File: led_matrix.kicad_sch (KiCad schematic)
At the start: 128 parts

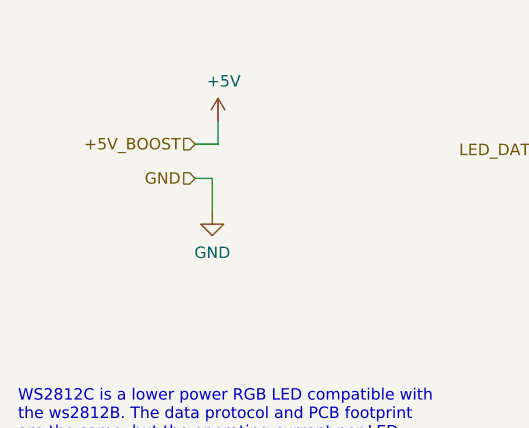
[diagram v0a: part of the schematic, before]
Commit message: Removes boost converter placeholder since it won't be possible to use it
The stamp can only provide 500mA@3.3v, which gives us 1.65W. Assuming a
85% efficiency of the boost regulator, that would give us 1.4W on the
output, or 280mA@5V. We need 320mA to run the 64 WS2812C, so it doesn't
seem to be possible to run these from a LiPO battery unless we rely on
the software never running all the LEDs at full brightness, but that
doesn't seem like a reliable option.

We'll still use the WS2812C instead of the B for the lower power
consumption, though. Since we don't need a lot of brightness, running
the matrix with 320mA should make it possible for the whole thing to run
from a standard USB connection.
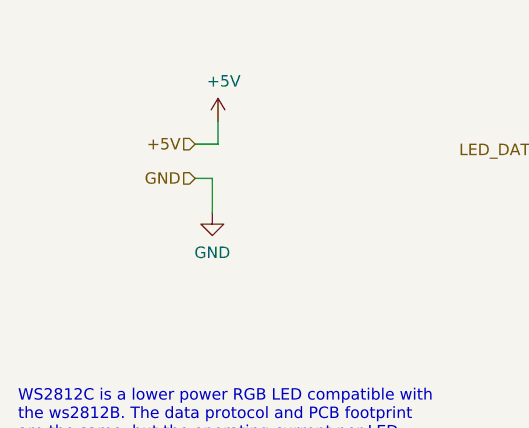
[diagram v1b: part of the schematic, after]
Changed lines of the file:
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@@
     (effects (font (size 1.27 1.27)) (justify left bottom))
   )
-  (hierarchical_label "+5V_BOOST" (shape input) (at 43.815 29.21 180)
+  (hierarchical_label "+5V" (shape input) (at 43.815 29.21 180)
     (effects (font (size 1.27 1.27)) (justify right))
   )

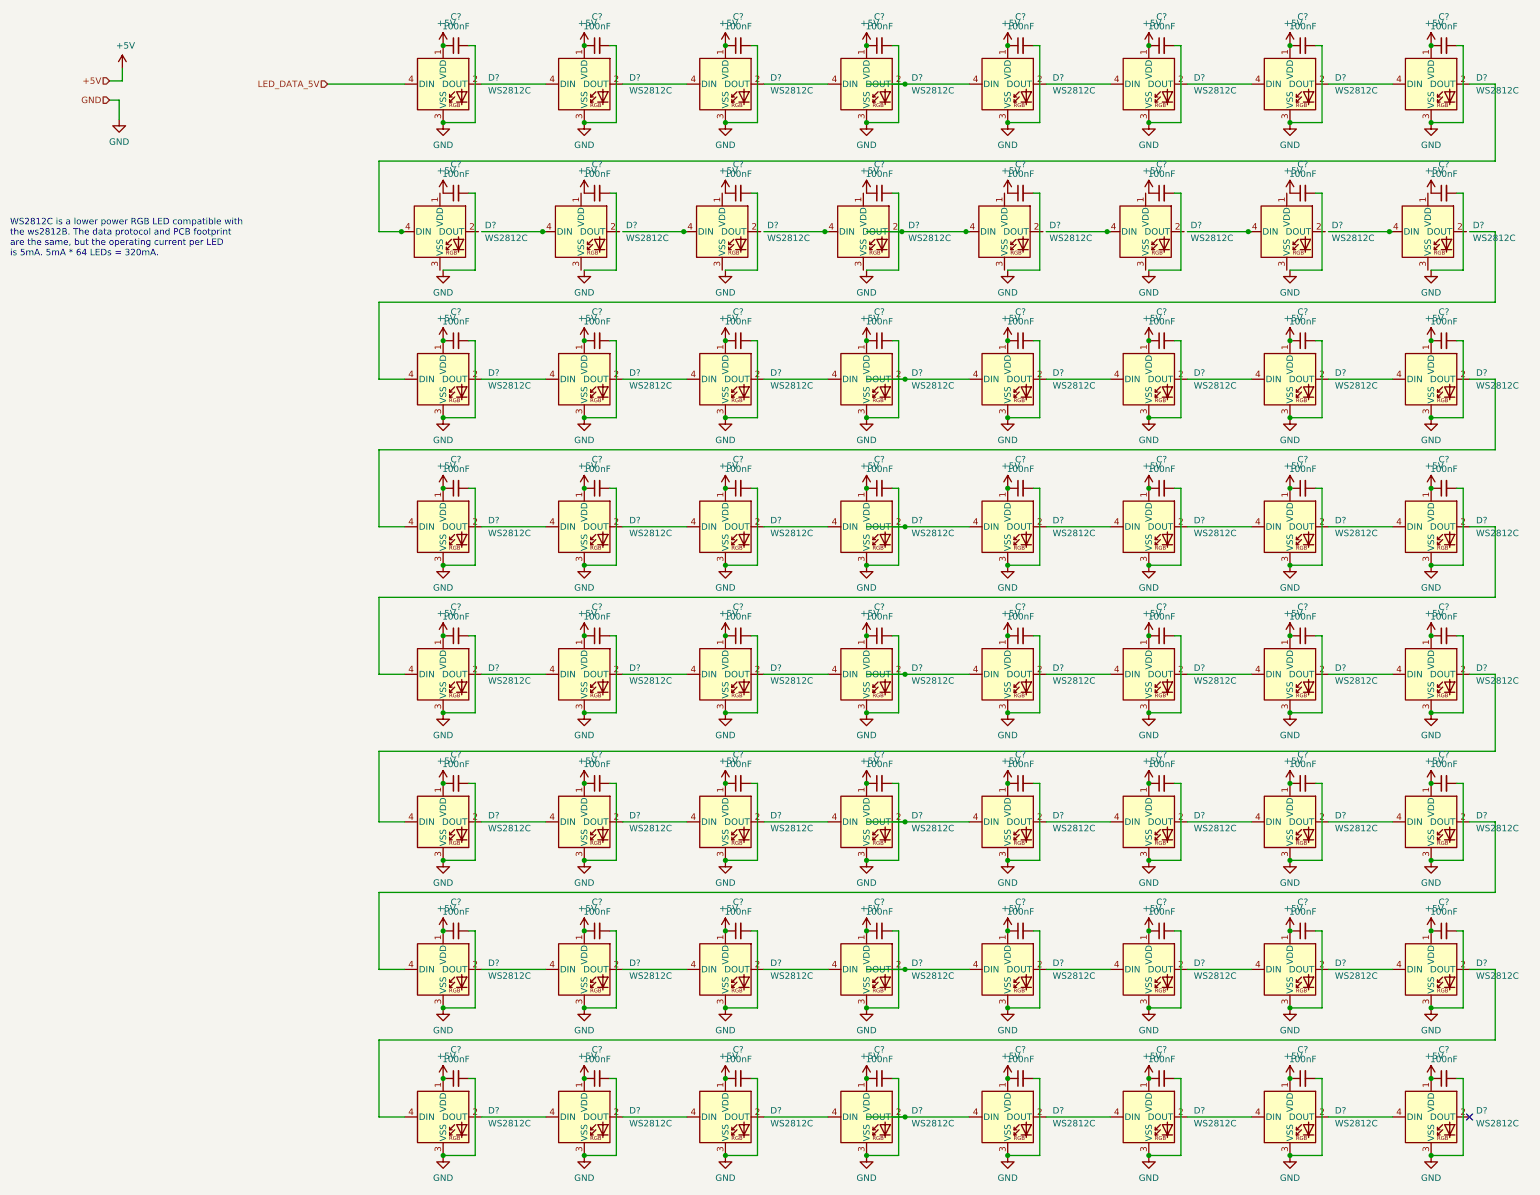
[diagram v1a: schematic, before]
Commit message: Annotates components on schematics
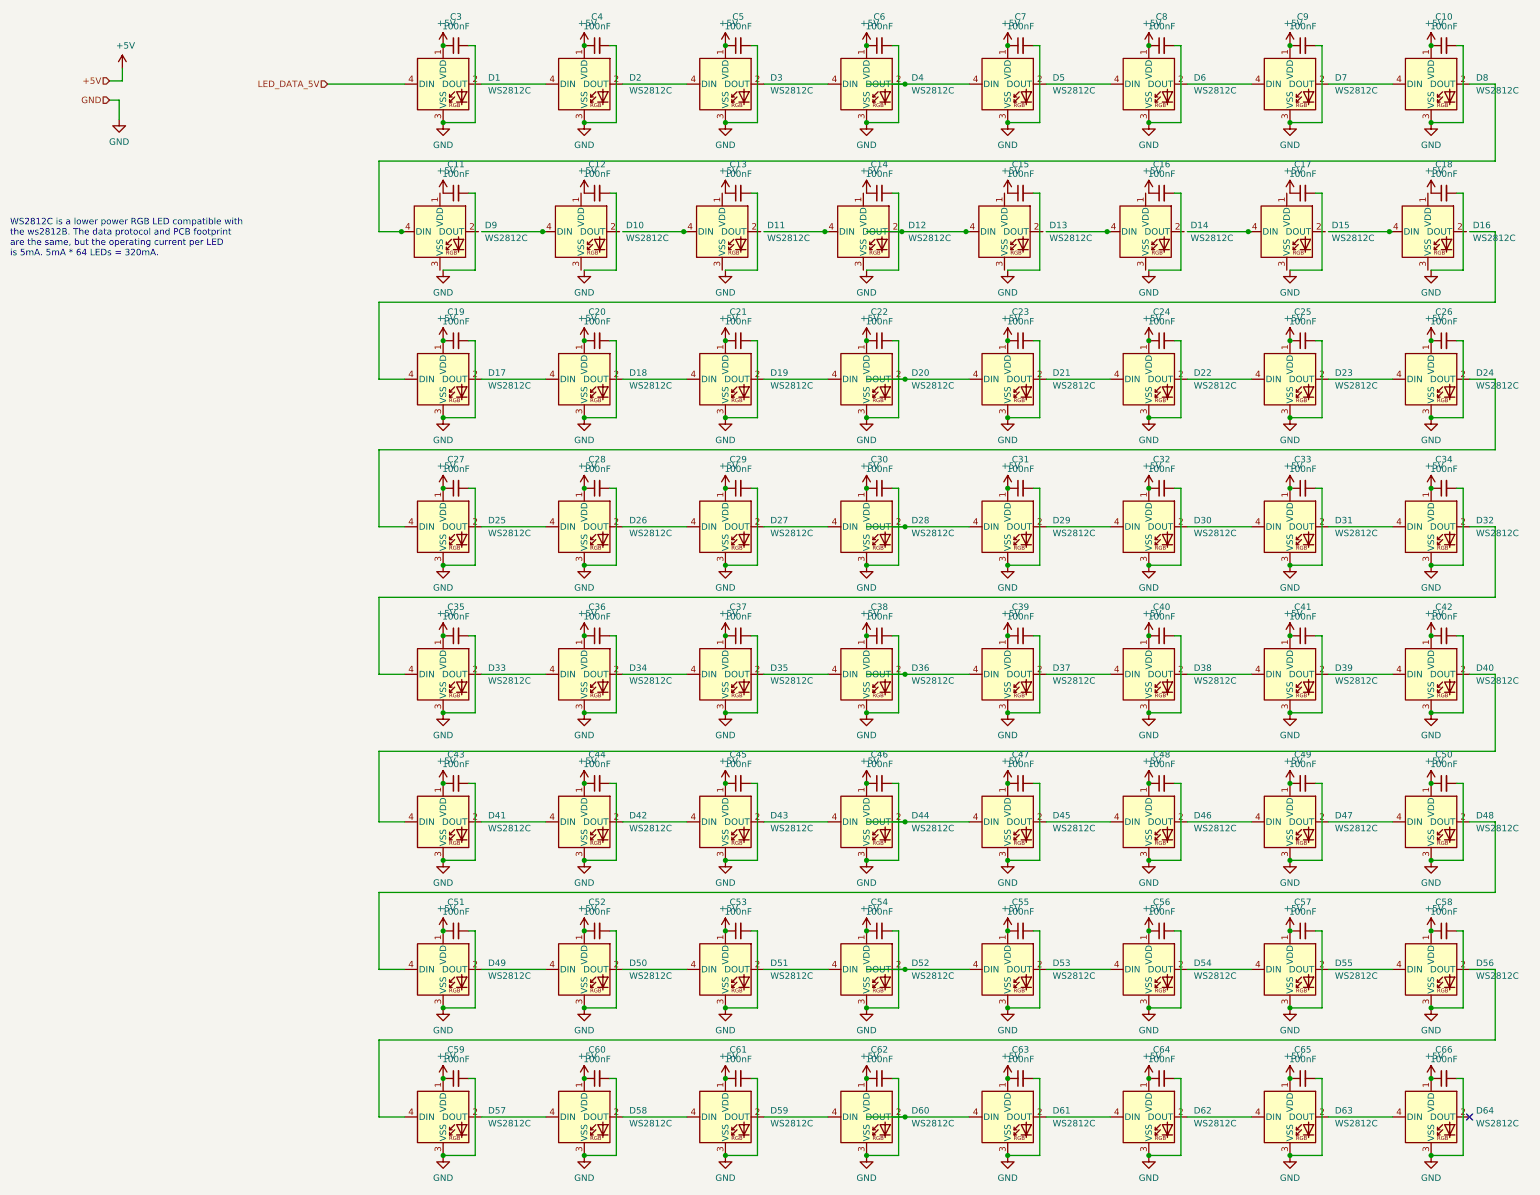
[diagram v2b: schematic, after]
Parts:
- gave numbers to parts that had none: 128

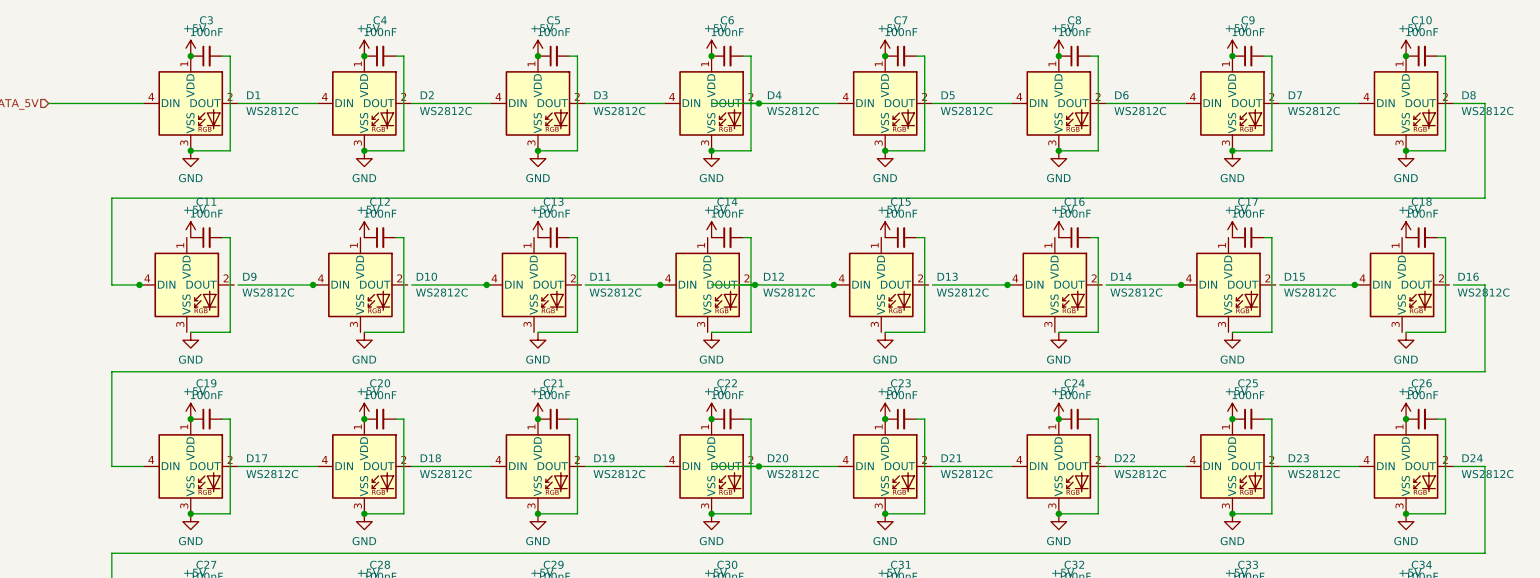
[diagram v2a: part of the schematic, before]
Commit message: Fixes ERC errors in the LED matrix schematics
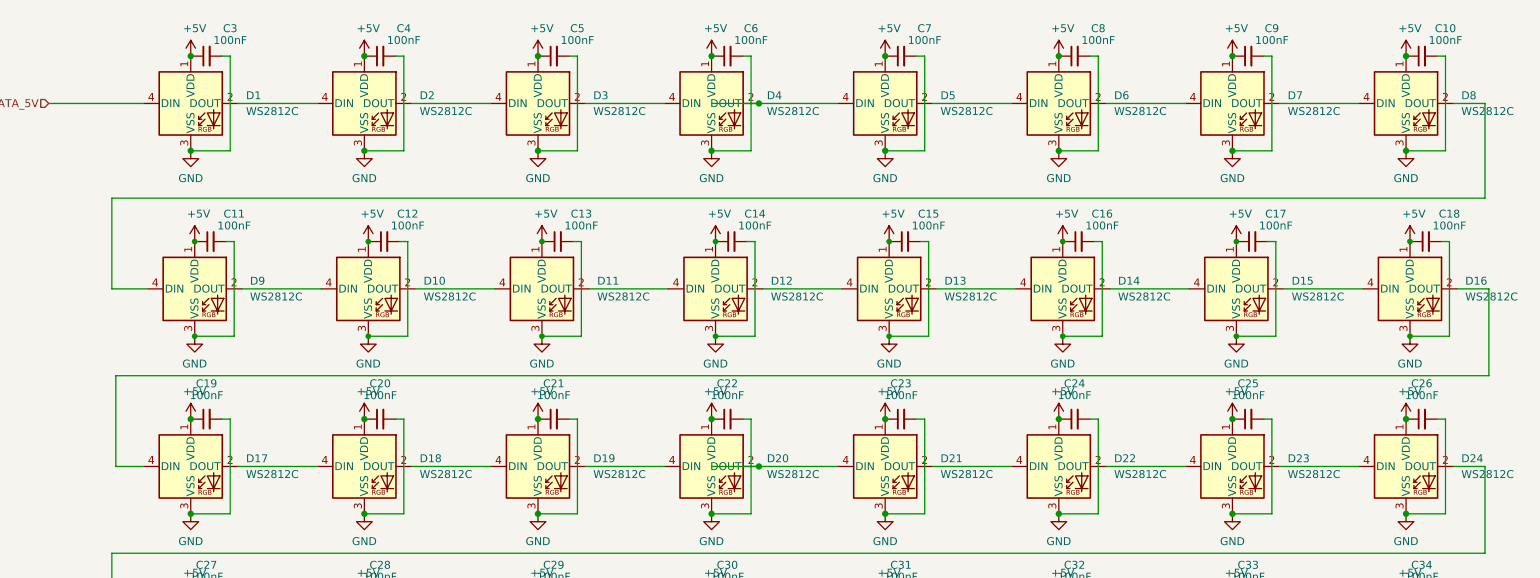
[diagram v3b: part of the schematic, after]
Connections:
- net +5V: now also D10.1 (VDD), D11.1 (VDD), D12.1 (VDD), D13.1 (VDD), D14.1 (VDD), D15.1 (VDD), D16.1 (VDD), D9.1 (VDD)
- net GND: now also D10.3 (VSS), D11.3 (VSS), D12.3 (VSS), D13.3 (VSS), D14.3 (VSS), D15.3 (VSS), D16.3 (VSS), D9.3 (VSS)
- net at D15.2 (DOUT): now also D16.4 (DIN)
- net at D15.4 (DIN): now also D14.2 (DOUT)
- net at D17.4 (DIN): now also D16.2 (DOUT)
- net at D9.2 (DOUT): now also D10.4 (DIN)
- net at D12.4 (DIN): now also D11.2 (DOUT)
- net at D11.4 (DIN): now also D10.2 (DOUT)
- net at D14.4 (DIN): now also D13.2 (DOUT)
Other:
- moved on the sheet: C11, C12, C13, C14, C15, C16, C17, C18, D10, D11, D12, D13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

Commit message: Associates capacitors to the correct footprint
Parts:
- C10, C11, C12, C13, C14, C15, C16, C17, C18, C19, C20, C21, C22, C23, C24, C25, C26, C27, C28, C29, C3, C30, C31, C32, C33, C34, C35, C36, C37, C38, C39, C4, C40, C41, C42, C43, C44, C45, C46, C47, C48, C49, C5, C50, C51, C52, C53, C54, C55, C56, C57, C58, C59, C6, C60, C61, C62, C63, C64, C65, C66, C7, C8, C9: footprint Capacitor_SMD:C_0805_2012Metric_Pad1.15x1.40mm_HandSolder -> Capacitor_SMD:C_0805_2012Metric_Pad1.18x1.45mm_HandSolder

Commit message: Adds project name and revision to schematics
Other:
- title: (none) -> Neopixel pico arcade - LED matrix
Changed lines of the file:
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@@
 (kicad_sch (version 20210621) (generator eeschema)
   (paper "A3")
+  (title_block
+    (title "Neopixel pico arcade - LED matrix")
+    (rev "1.0")
+  )
   (junction (at 109.855 22.225) (diameter 1.016) (color 0 0 0 0))
   (junction (at 109.855 37.465) (diameter 1.016) (color 0 0 0 0))

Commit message: Uses a copy of the built-in WS2812B footprint but with hidden silkscreen
Since this will be the screen, it's better to have no visible silkscreen.
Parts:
- D1, D10, D11, D12, D13, D14, D15, D16, D17, D18, D19, D2, D20, D21, D22, D23, D24, D25, D26, D27, D28, D29, D3, D30, D31, D32, D33, D34, D35, D36, D37, D38, D39, D4, D40, D41, D42, D43, D44, D45, D46, D47, D48, D49, D5, D50, D51, D52, D53, D54, D55, D56, D57, D58, D59, D6, D60, D61, D62, D63, D64, D7, D8, D9: footprint LED_SMD:LED_WS2812B_PLCC4_5.0x5.0mm_P3.2mm -> Neopixel_pico_arcade:LED_WS2812C_HIDDEN_SILKSCREEN_5.0x5.0mm_P3.2mm

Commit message: Adds a copy of the built-in 0805 capacitor footprint with no silkscreen
For the same reason we hid the LED silkscreen.
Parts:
- C10, C11, C12, C13, C14, C15, C16, C17, C18, C19, C20, C21, C22, C23, C24, C25, C26, C27, C28, C29, C3, C30, C31, C32, C33, C34, C35, C36, C37, C38, C39, C4, C40, C41, C42, C43, C44, C45, C46, C47, C48, C49, C5, C50, C51, C52, C53, C54, C55, C56, C57, C58, C59, C6, C60, C61, C62, C63, C64, C65, C66, C7, C8, C9: footprint Capacitor_SMD:C_0805_2012Metric_Pad1.18x1.45mm_HandSolder -> Neopixel_pico_arcade:C_0805_hidden_silkscreen_2012Metric_Pad1.18x1.45mm_HandSolder
